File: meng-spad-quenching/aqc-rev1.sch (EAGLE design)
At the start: 138 parts, among them IC1 ADCMP582, IC2 NC7SV74K8X, IC3 LT3032-5, IC4 OPA342, IC5 OPA342, IC6 LTC1711, IC7 DS1100LU-20+, IC8 LT3032-15, IC9 NC7WZ16P6X, J1 VIN_LOGIC, M1 BSS806N, Q1 MMBTH81, Q2 MMBTH81, Q3 MMBTH81, Q4 MMBTH81, Q5 MMBTH81, Q6 MMBTH81, SW1 CJS-1200TB, SW2 CJS-1200TB, SW3 CJS-1200TB, T1 MMBTH10, T2 MMBTH10, T3 MMBTH10, T4 MMBTH10, T5 MMBTH10, T6 MMBTH10, T7 MMBTH10, U1 SN65EPT21DGK, U2 TPS78233DDCT, U3 SN65EPT22DGK, X1 CONN_SPAD, X2 CONN_PHOTON_COUNTER, X3 CONN_FORCE_QUENCH, X4 CONN_VREF_ONE_SHOT_EXT, X5 CONN_VREF_DIAMOND_IBIAS_EXT, X6 CONN_VREF_CASCODE_IBIAS_EXT

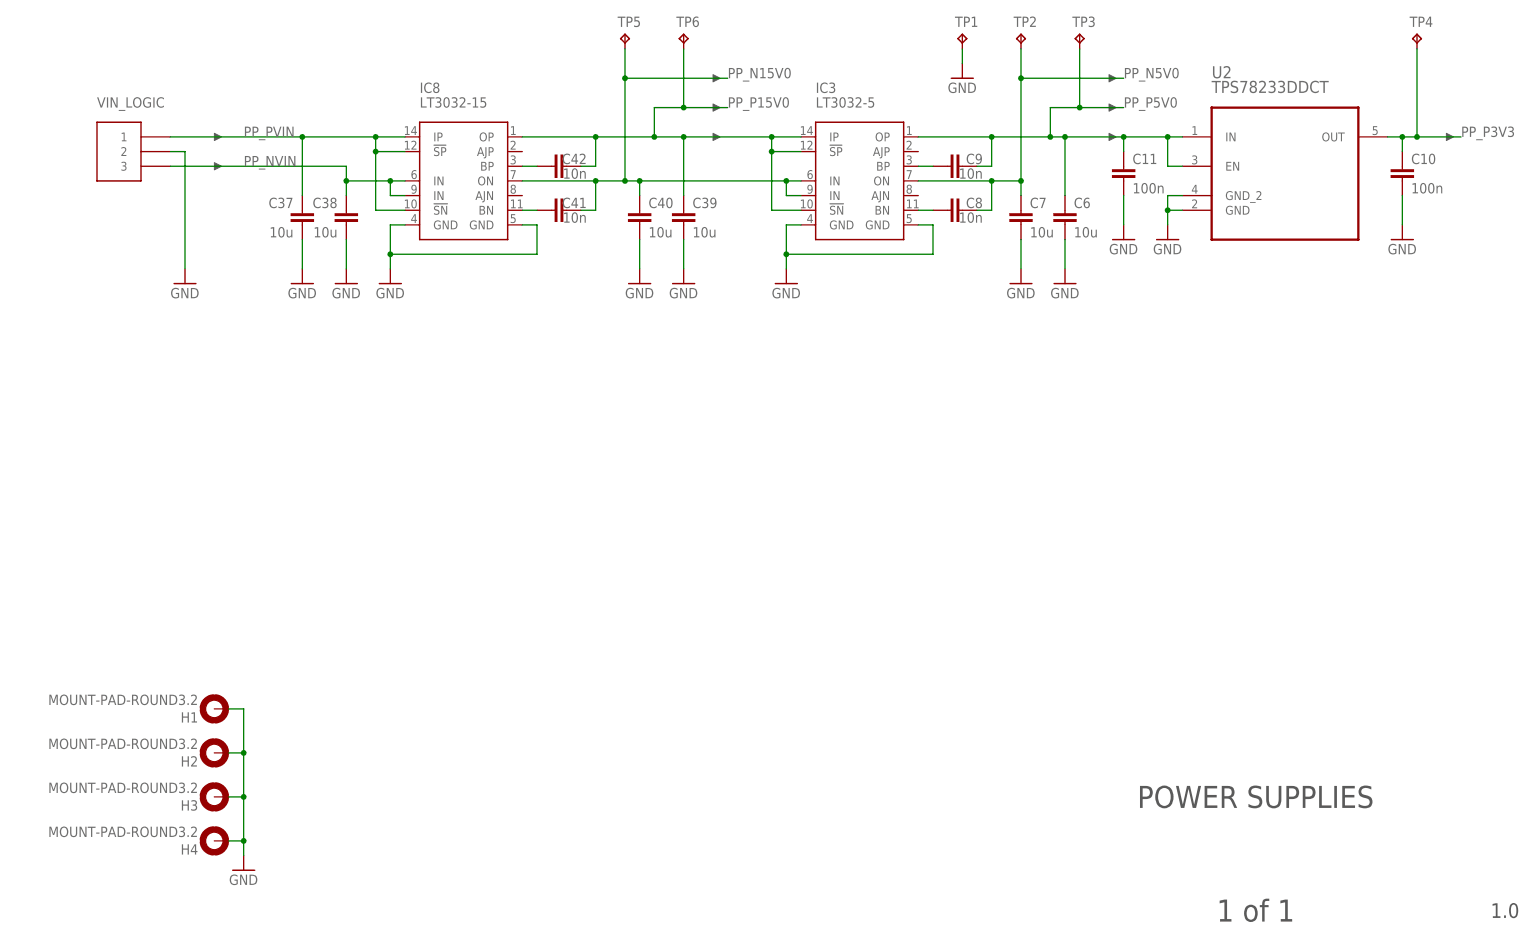
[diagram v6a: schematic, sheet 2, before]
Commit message: Added VREF testpts, routed, exported gerbers
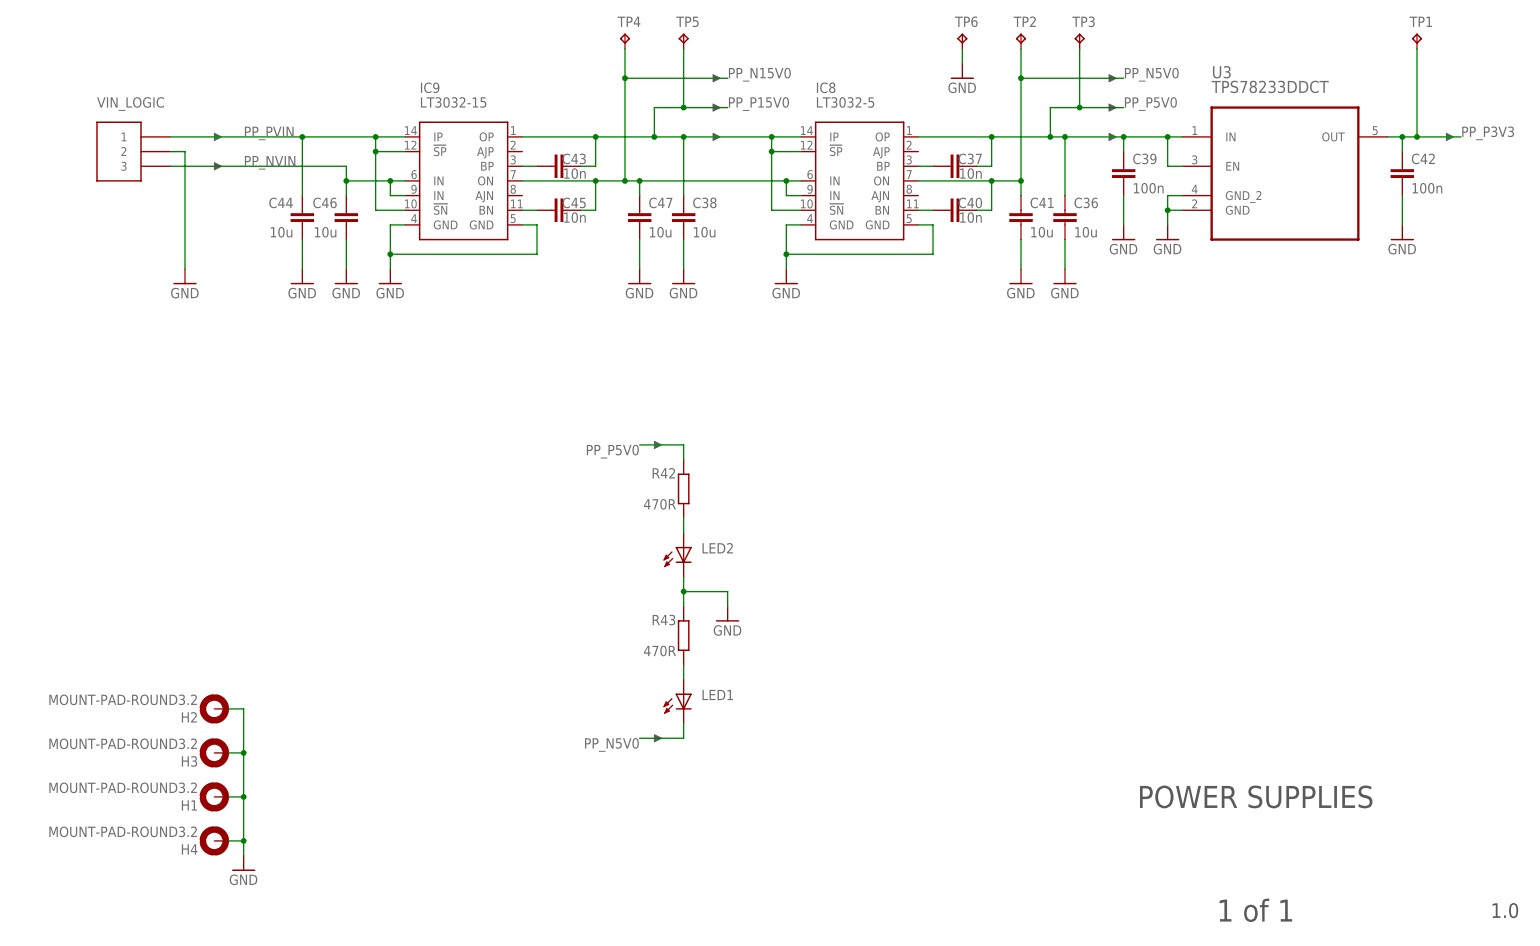
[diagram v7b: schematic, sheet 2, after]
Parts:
- removed R47: 49R9, rcl:R-EU_R0603
- added C47: 10u, rcl:C-EUC1206
- added LED1, LED2: (no value), led:LEDCHIP-LED0805
- added R35, R40: DNP, rcl:R-EU_R0603
- added R43: 470R, resistor:R-EU_R0805
- added TP10, TP13: GND, Kramnik's Library:KEYSTONE_5000
- added TP11: TPTP08R, testpad:TPTP08R
- added TP12: VREF_AV_DET, Kramnik's Library:KEYSTONE_5000
- added TP7: VREF_ONE_SHOT, Kramnik's Library:KEYSTONE_5000
- added TP8: VREF_DIAMOND_IBIAS, Kramnik's Library:KEYSTONE_5000
- added TP9: VREF_CASCODE_IBIAS, Kramnik's Library:KEYSTONE_5000
- C10, C16, C18, C25, C3, C35: value 100n -> 10n
- C11, C26, C31, C32: device rcl:C-EUC0603 -> rcl:C-EUC0402
- C14, C43, C45: device rcl:C-EUC0402 -> rcl:C-EUC0603
- C15: value 10n -> 100n; device rcl:C-EUC0402 -> rcl:C-EUC0603
- C19, C24, C34, C42: value 10n -> 100n
- C20: value 1n -> 100n; device rcl:C-EUC0603 -> rcl:C-EUC0402
- C21, C8: value 10n -> 100n; device rcl:C-EUC0603 -> rcl:C-EUC0402
- C23: value 100n -> 1n; device rcl:C-EUC0402 -> rcl:C-EUC0603
- C33: value 33u, 25V -> 10n; device rcl:CPOL-EUCT7343 -> rcl:C-EUC0402
- C36, C44: value 100n -> 10u; device rcl:C-EUC0402 -> rcl:C-EUC1206
- C37, C40, C6: value 10u -> 10n; device rcl:C-EUC1206 -> rcl:C-EUC0603
- C39, C7: value 10u -> 100n; device rcl:C-EUC1206 -> rcl:C-EUC0603
- C41: value 10n -> 10u; device rcl:C-EUC0603 -> rcl:C-EUC1206
- C46: value 10n -> 10u; device rcl:C-EUC0402 -> rcl:C-EUC1206
- C9: value 10n -> 33u, 25V; device rcl:C-EUC0603 -> rcl:CPOL-EUCT7343
- IC2: value NC7SV74K8X -> OPA342; device meng:NC7SV74K8X -> meng:OPA333DBV
- IC3: value LT3032-5 -> NC7SV74K8X; device meng:LT3032 -> meng:NC7SV74K8X
- IC5: value OPA342 -> NC7WZ16P6X; device meng:OPA333DBV -> meng:NC7WZ16P6X
- IC8: value LT3032-15 -> LT3032-5
- IC9: value NC7WZ16P6X -> LT3032-15; device meng:NC7WZ16P6X -> meng:LT3032
- R1, R29: value 470R -> DNP
- R10, R9: value 150R -> 49R9; device rcl:R-EU_R0402 -> rcl:R-EU_R0603
- R11: value 49R9 -> 1k43
- R12: value DNP -> 470R
- R13: value 0R -> 49R9
- R14, R5: value DNP -> 1k
- R15: value DNP -> 10k
- R16: value 470R -> 1k
- R17, R6: value 49R9 -> 1k
- R18, R19: value 49R9 -> 470R
- R2: value DNP -> 49R9
- R20: value 49R9 -> 0R
- R21: value 49R9 -> DNP
- R22: value 1k -> 49R9
- R23: value 1k -> 470R
- R24: value 1k -> 100R; device rcl:R-EU_R0603 -> rcl:R-EU_R0402
- R25: value 1k -> 100R
- R26: value 1k -> 10k
- R27: value 470R -> 49R9
- R28: value 1k43 -> 49R9
- R3: value 10k -> 49R9
- R30: value 100R -> DNP
- R31: value 10k -> DNP
- R42: value DNP -> 470R; device rcl:R-EU_R0603 -> resistor:R-EU_R0805
- R7: value DNP -> 150R; device rcl:R-EU_R0603 -> rcl:R-EU_R0402
- R8: value 100R -> 150R
- U2: value TPS78233DDCT -> SN65EPT22DGK; device Texas Instruments_By_element14_Batch_1 (2):TPS78233DDCT -> Texas Instruments_By_element14_Batch_1:SN65EPT22DGK
- U3: value SN65EPT22DGK -> TPS78233DDCT; device Texas Instruments_By_element14_Batch_1:SN65EPT22DGK -> Texas Instruments_By_element14_Batch_1 (2):TPS78233DDCT
- X3: value CONN_FORCE_QUENCH -> CONN_VREF_CASCODE_IBIAS_EXT; MF JOHNSON COMPONENTS -> (none); MPN 142-0711-871 -> (none); OC_FARNELL unknown -> (none); OC_NEWARK 01C1639 -> (none)
- X4: value CONN_VREF_ONE_SHOT_EXT -> CONN_VREF_DIAMOND_IBIAS_EXT
- X5: value CONN_VREF_DIAMOND_IBIAS_EXT -> CONN_VREF_ONE_SHOT_EXT
- X6: value CONN_VREF_CASCODE_IBIAS_EXT -> CONN_FORCE_QUENCH; MF (none) -> JOHNSON COMPONENTS; MPN (none) -> 142-0711-871; OC_FARNELL (none) -> unknown; OC_NEWARK (none) -> 01C1639
- renumbered D2 to D1, R45 to R39, R46 to R36
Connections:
- new net N$39: LED1.A, R43.1
- new net N$40: LED2.A, R42.1
- net !FORCE_QUENCH: now also IC3.!PRE, R22.1, X6G1.1; no longer IC2.!PRE, R6.1, X3G1.1
- net !ONE_SHOT_CLR: now also IC3.!CLR; no longer IC2.!CLR
- net BLANKING_LATCH_EN: now also R29.1, R30.1, R34.1, R35.1, U2.D0; no longer R12.1, R2.1, R33.1, R5.1, U3.D0
- net COMP_LE_N: now also U2.Q0; no longer U3.Q0
- net COMP_LE_P: now also U2.~Q0; no longer U3.~Q0
- net COMP_Q_N: now also R24.1, R7.1; no longer R10.1, R8.1
- net COMP_Q_P: now also R24.2, R8.1; no longer R8.2, R9.1
- net GND: now also C26.2, C33.2, C41.2, C42.2, C47.2, C8.2, C9.-, IC2.V-, IC4.V+, IC5.GND, IC9.GND@1, LED2.C, Q4.C, R1.1, R17.1, R2.2, R21.2, R33.1, R40.2, R43.2, R5.1, R7.2, R8.2, TP10.P$1, TP13.P$1, TP6.TP, U2.D1, U3.GND_2; no longer C33.-, C37.2, C40.2, C43.2, C45.2, C6.2, IC2.GND, IC3.GND@1, IC4.V-, IC5.V+, Q2.C, R10.2, R11.2, R15.1, R22.1, R23.1, R24.1, R34.2, R37.2, R9.2, TP1.TP, U2.GND_2, U3.D1
- net HOLDOFF_TRIG: now also IC3.CLK; no longer IC2.CLK
- net LOGIC_QUENCH: now also IC3.Q, IC5.IN1, IC5.IN2, R20.2, R23.2; no longer IC2.Q, IC9.IN1, IC9.IN2, R13.2, R16.2
- net LOGIC_QUENCH_ATTEN: now also R20.1, R21.1, T7.B; no longer R13.1, R34.1, T6.B
- net N$1: now also R34.2; no longer R33.2
- net N$10: now also Q2.C, Q3.E; no longer Q1.C, Q6.E
- net N$11: now also Q5.E, R9.1; no longer Q2.E, R18.1
- net N$12: now also C6.1, Q1.C, R9.2, T1.B; no longer C26.1, Q3.C, R18.2, T2.B
- net N$13: now also R10.2, T2.E; no longer R20.2, T1.E
- net N$14: now also Q2.E, R4.1; no longer Q1.E, R19.1
- net N$15: now also T7.C; no longer T6.C
- net N$16: now also IC2.OUT; no longer IC4.OUT
- net N$17: now also R32.2; no longer R12.2
- net N$18: now also Q4.B, Q6.C, R11.2; no longer Q4.C, Q5.B, R28.2
- net N$19: now also C6.2, Q2.B, R10.1; no longer C26.2, Q1.B, R20.1
- net N$2: now also R28.1; no longer R4.1
- net N$20: now also R14.2; no longer R23.2
- net N$21: now also Q5.B, R13.1, T2.B; no longer Q2.B, R21.1, T1.B
- net N$22: now also R12.1, R13.2; no longer R1.1, R21.2
- net N$23: now also IC2.-IN, R17.2; no longer IC4.-IN, R24.2
- net N$24: now also R19.2, T6.C, T7.E; no longer R27.2, T6.E, T7.C
- net N$25: now also R25.1, R26.2; no longer R30.1, R31.2
- net N$26: now also Q1.E, R6.1; no longer Q3.E, R25.1
- net N$27: now also R11.1; no longer R28.1
- net N$28: now also R29.2; no longer R5.2
- net N$29: now also Q6.E, R16.1; no longer Q4.E, R26.1
- net N$3: now also R1.2; no longer R15.2
- net N$30: now also IC4.OUT, T6.B; no longer IC5.OUT, T7.B
- net N$31: now also Q1.B, Q4.E, Q6.B; no longer Q3.B, Q4.B, Q5.E
- net N$32: now also R35.2; no longer R2.2
- net N$33: now also C43.1, IC9.BP; no longer C42.1, IC8.BP
- net N$34: now also C45.1, IC9.BN; no longer C41.1, IC8.BN
- net N$35: now also IC4.-IN, R18.2, T6.E; no longer IC5.-IN, R29.2, T7.E
- net N$36: now also R27.2; no longer R47.2
- net N$37: now also IC5.OUT1, IC5.OUT2, R28.2; no longer IC9.OUT1, IC9.OUT2, R4.2
- net N$4: now also R15.2; no longer R3.2
- net N$5: now also R3.2, T1.E; no longer R17.2, T2.E
- net N$6: now also R2.1; no longer R11.1
- net N$7: now also R30.2; no longer R32.2
- net N$8: now also C37.1, IC8.BP; no longer C9.1, IC3.BP
- net N$9: now also C40.1, IC8.BN; no longer C8.1, IC3.BN
- net NC_!LOGIC_QUENCH: now also IC3.!Q, TP11.TP; no longer IC2.!Q
- net ONE_SHOT_CAP: now also C23.1, R23.1, R25.2; no longer C20.1, R16.1, R30.2
- net ONE_SHOT_CLR: now also R26.1, R27.1; no longer R31.1, R47.1
- net PP_N15V0: now also C45.2, C47.1, IC8.IN, IC8.IN@1, IC9.ON, TP4.TP; no longer C40.1, C41.2, IC3.IN, IC3.IN@1, IC8.ON, TP5.TP
- net PP_N5V0: now also C12.1, C13.1, C25.1, C28.1, C40.2, C41.1, IC4.V-, IC8.ON, LED1.C, R15.1, R18.1, R19.1, R36.1, RT2.1; no longer C18.1, C19.1, C29.1, C30.1, C7.1, C8.2, IC3.ON, IC5.V-, R27.1, R29.1, R3.1
- net PP_NVIN: now also C46.1, IC9.IN, IC9.IN@1; no longer C38.1, IC8.IN, IC8.IN@1
- net PP_P15V0: now also C1.1, C14.1, C3.1, C38.1, C43.2, C9.+, IC8.!SN, IC8.!SP, IC8.IP, IC9.OP, R12.2, R16.2, R6.2, TP5.TP; no longer C31.1, C32.1, C33.+, C39.1, C42.2, IC3.!SN, IC3.!SP, IC3.IP, IC8.OP, R1.2, R25.2, R26.2, TP6.TP
- net PP_P3V3: now also C19.1, C21.1, C27.1, C30.1, C31.1, C32.1, C33.1, C4.1, C42.1, C8.1, IC3.D, IC3.VDD, IC5.VCC, R22.2, TP1.TP, U2.VCC, U3.OUT; no longer C10.1, C12.1, C13.1, C17.1, C2.1, C23.1, C25.1, C36.1, C43.1, C44.1, IC2.D, IC2.VDD, IC9.VCC, R36.1, R6.2, RT2.1, TP4.TP, U2.OUT, U3.VCC
- net PP_P5V0: now also C17.1, C2.1, C20.1, C36.1, C37.2, C39.1, C7.1, IC2.V+, IC8.OP, Q3.B, R31.2, R37.1, R42.2, U3.EN, U3.IN; no longer C1.1, C14.1, C27.1, C28.1, C3.1, C6.1, C9.2, IC3.OP, IC4.V+, Q6.B, R42.1, R7.2, U2.EN, U2.IN
- net PP_PVIN: now also C44.1, IC9.!SN, IC9.!SP, IC9.IP; no longer C37.1, IC8.!SN, IC8.!SP, IC8.IP
- net SPAD_PULLDN_SENSE: now also Q3.C, R5.2; no longer Q6.C, R22.2
- net VREF_AV_DET: now also C10.1, R31.1, R33.2, TP12.P$1; no longer C21.1, R14.2, R7.1
- net VREF_CASCODE_IBIAS: now also C26.1, IC4.+IN, SW1.COM, TP9.P$1; no longer C45.1, IC5.+IN, SW3.COM
- net VREF_CASCODE_IBIAS_EXT: now also SW1.NO, X3G1.1; no longer SW3.NO, X6G1.1
- net VREF_CASCODE_IBIAS_INT: now also RT2.2, SW1.NC; no longer RT4.2, SW3.NC
- net VREF_DIAMOND_IBIAS: now also C18.1, IC2.+IN, TP8.P$1; no longer C46.1, IC4.+IN
- net VREF_DIAMOND_IBIAS_EXT: now also X4G1.1; no longer X5G1.1
- net VREF_DIAMOND_IBIAS_INT: now also R37.2, R40.1; no longer R41.1, R42.2
- net VREF_ONE_SHOT: now also C29.1, SW3.COM, TP7.P$1; no longer C4.1, SW1.COM
- net VREF_ONE_SHOT_EXT: now also SW3.NO, X5G1.1; no longer SW1.NO, X4G1.1
- net VREF_ONE_SHOT_INT: now also R41.1, RT4.2, SW3.NC; no longer R37.1, RT2.2, SW1.NC
- net VSPAD: now also R3.1, R4.2; no longer R17.1, R19.2
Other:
- moved on the sheet: C1, C12, C13, C16, C19, C26, C28, C3, C34, C35, C37, C38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

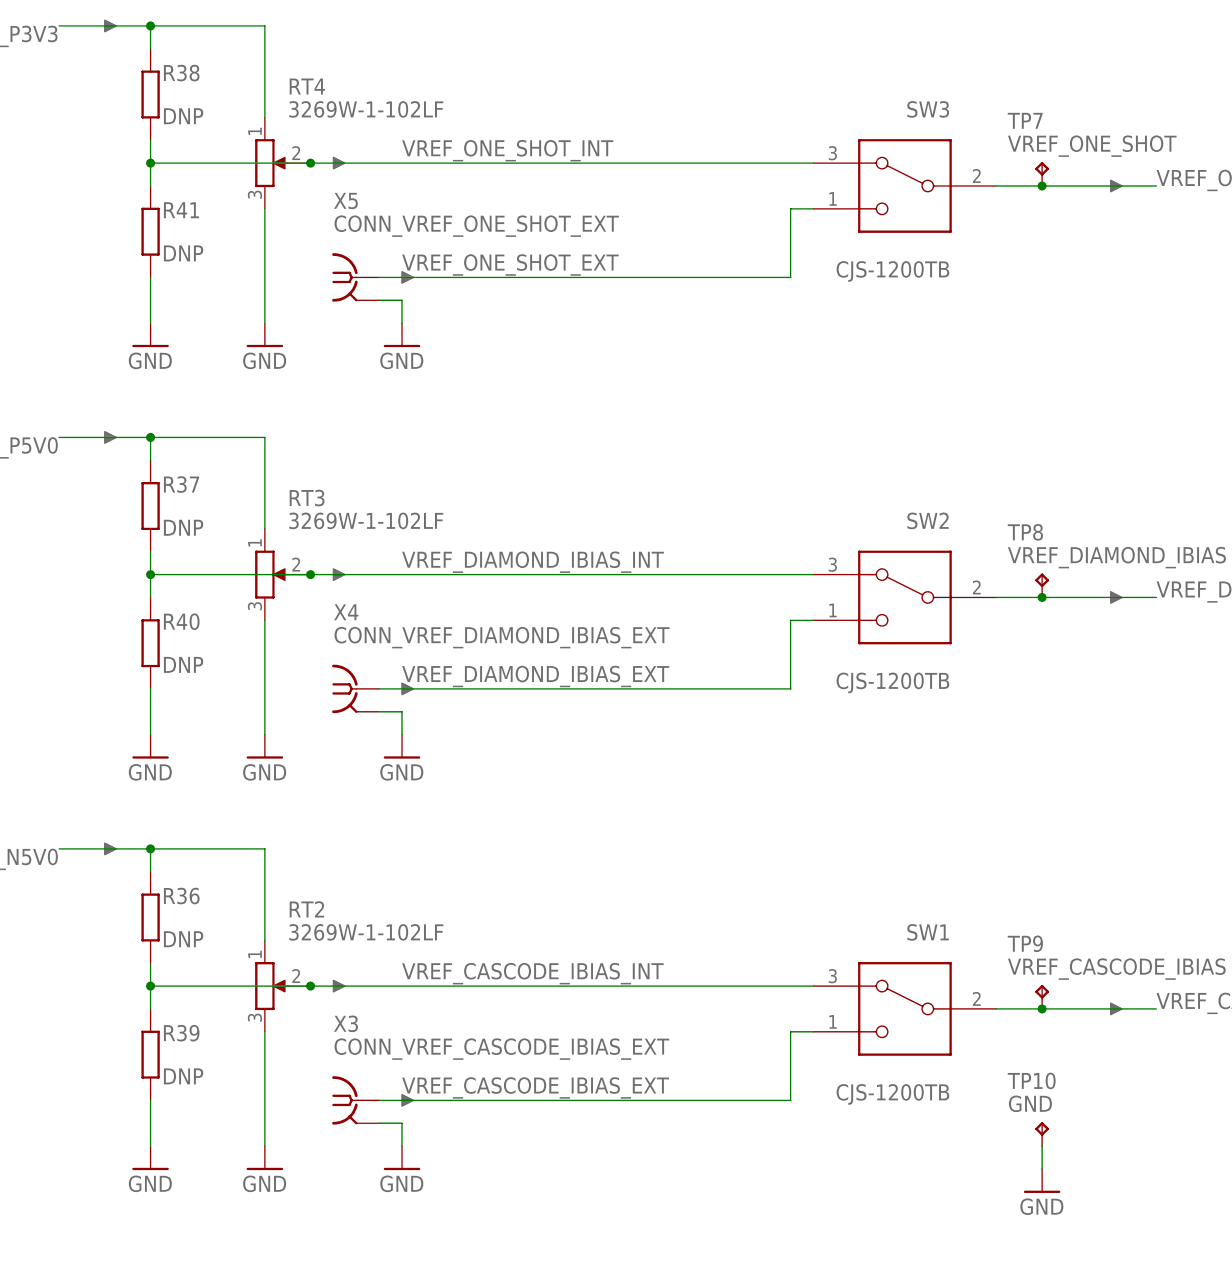
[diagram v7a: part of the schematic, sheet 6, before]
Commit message: Renumbered, moved some refdes, checked and approved all DRC violations, exported gerbers
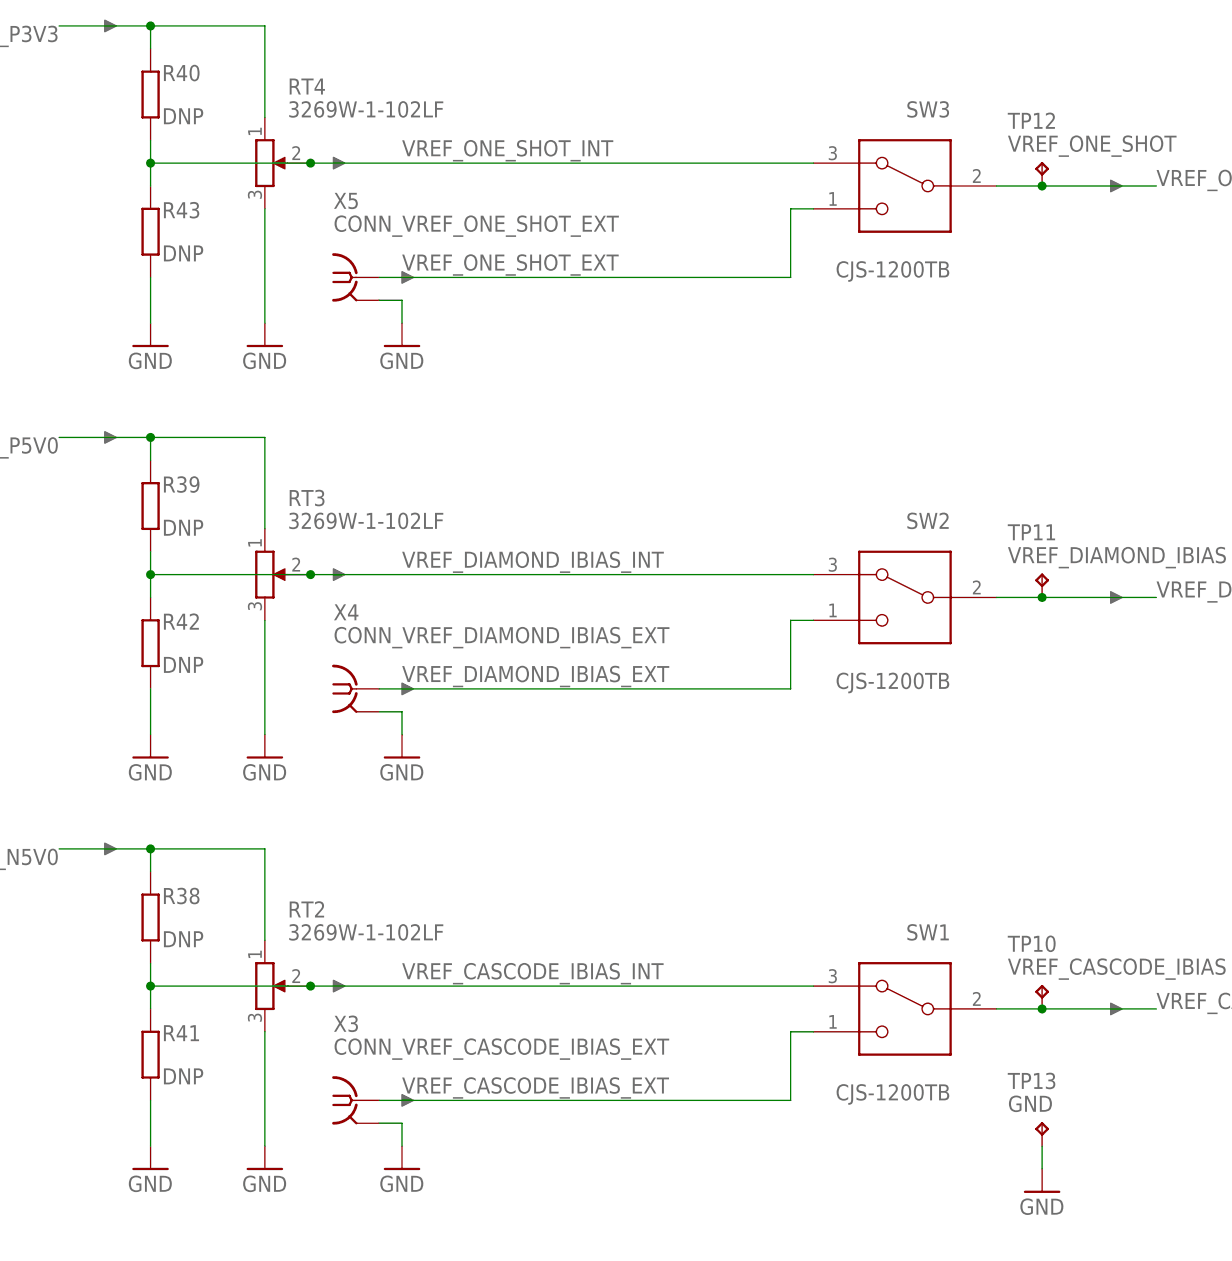
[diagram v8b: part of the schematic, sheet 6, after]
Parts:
- R36, R37: value DNP -> 470R; device rcl:R-EU_R0603 -> resistor:R-EU_R0805
- R42, R43: value 470R -> DNP; device resistor:R-EU_R0805 -> rcl:R-EU_R0603
- TP1: value TPTP20R -> TPTP08R; device testpad:TPTP20R -> testpad:TPTP08R
- TP10: value GND -> VREF_CASCODE_IBIAS
- TP11: value TPTP08R -> VREF_DIAMOND_IBIAS; device testpad:TPTP08R -> Kramnik's Library:KEYSTONE_5000
- TP12: value VREF_AV_DET -> VREF_ONE_SHOT
- TP2: value TPTP20R -> VREF_AV_DET; device testpad:TPTP20R -> Kramnik's Library:KEYSTONE_5000
- TP3: value TPTP20R -> GND; device testpad:TPTP20R -> Kramnik's Library:KEYSTONE_5000
- TP7: value VREF_ONE_SHOT -> TPTP20R; device Kramnik's Library:KEYSTONE_5000 -> testpad:TPTP20R
- TP8: value VREF_DIAMOND_IBIAS -> TPTP20R; device Kramnik's Library:KEYSTONE_5000 -> testpad:TPTP20R
- TP9: value VREF_CASCODE_IBIAS -> TPTP20R; device Kramnik's Library:KEYSTONE_5000 -> testpad:TPTP20R
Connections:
- net GND: now also R36.2, R42.2, TP3.P$1, TP9.TP; no longer R39.2, R40.2, TP10.P$1, TP6.TP
- net N$39: now also R36.1; no longer R43.1
- net N$40: now also R37.1; no longer R42.1
- net NC_!LOGIC_QUENCH: now also TP1.TP; no longer TP11.TP
- net PP_N15V0: now also TP7.TP; no longer TP4.TP
- net PP_N5V0: now also R38.1, TP5.TP; no longer R36.1, TP2.TP
- net PP_P15V0: now also TP8.TP; no longer TP5.TP
- net PP_P3V3: now also R40.1, TP4.TP; no longer R38.1, TP1.TP
- net PP_P5V0: now also R37.2, R39.1, TP6.TP; no longer R37.1, R42.2, TP3.TP
- net VREF_AV_DET: now also TP2.P$1; no longer TP12.P$1
- net VREF_CASCODE_IBIAS: now also TP10.P$1; no longer TP9.P$1
- net VREF_CASCODE_IBIAS_INT: now also R38.2, R41.1; no longer R36.2, R39.1
- net VREF_DIAMOND_IBIAS: now also TP11.P$1; no longer TP8.P$1
- net VREF_DIAMOND_IBIAS_INT: now also R39.2, R42.1; no longer R37.2, R40.1
- net VREF_ONE_SHOT: now also TP12.P$1; no longer TP7.P$1
- net VREF_ONE_SHOT_INT: now also R40.2, R43.1; no longer R38.2, R41.1
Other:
- moved on the sheet: R38, R39, R40, R41, TP10, TP4, TP5, TP6
